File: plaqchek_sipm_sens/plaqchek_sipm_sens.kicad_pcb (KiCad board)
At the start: 2 copper layers, 90 parts, among them J2 Conn_01x04, J3 Conn_01x05, U1 TPS7A2050PDBVR, U10 AFBR-S4N44P014M, U11 LDK320AM-R, U2 OPA863A, U3 OPA863A, U4 OPA863A, U5 MCP1501T-50E, U6 MCP33131-10-E/MS, U7 MIC5504-1.8YM5, U8 RT9072BGB, U9 MC79M05_TO252

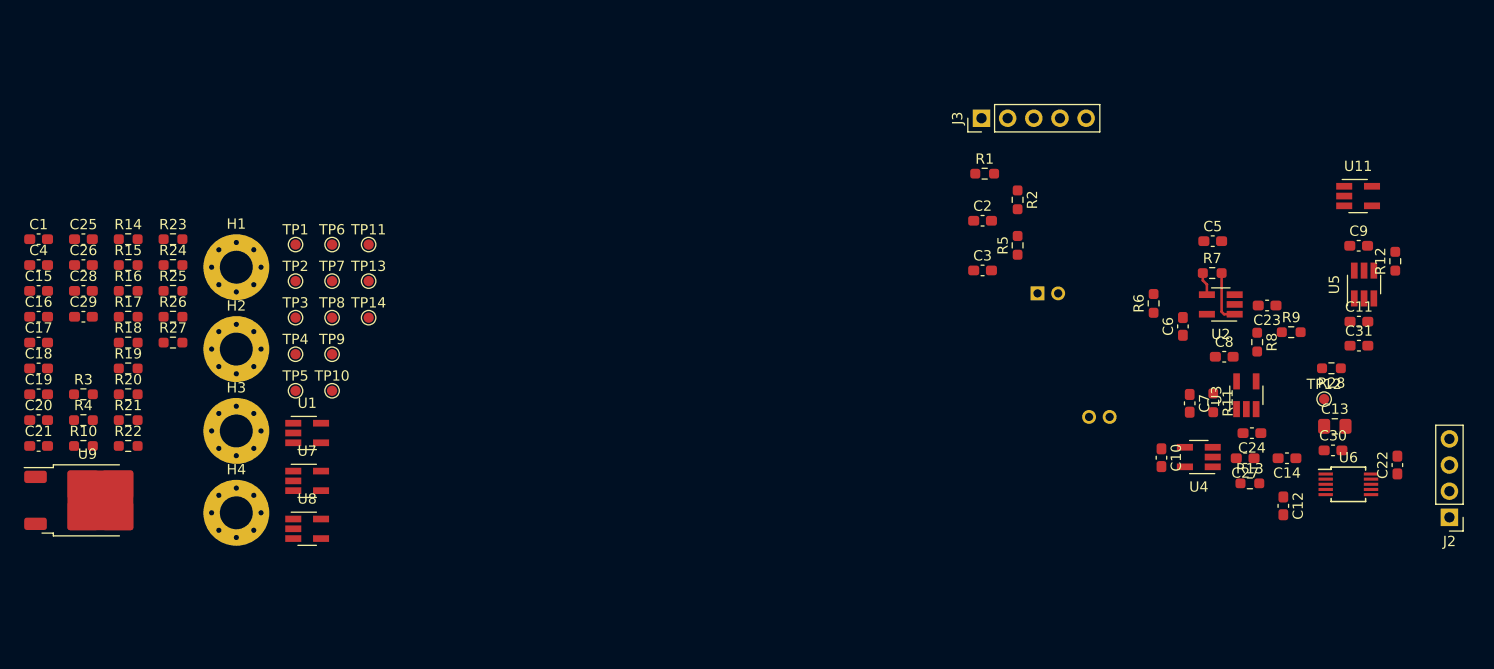
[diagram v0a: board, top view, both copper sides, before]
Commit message: start sensor board routing
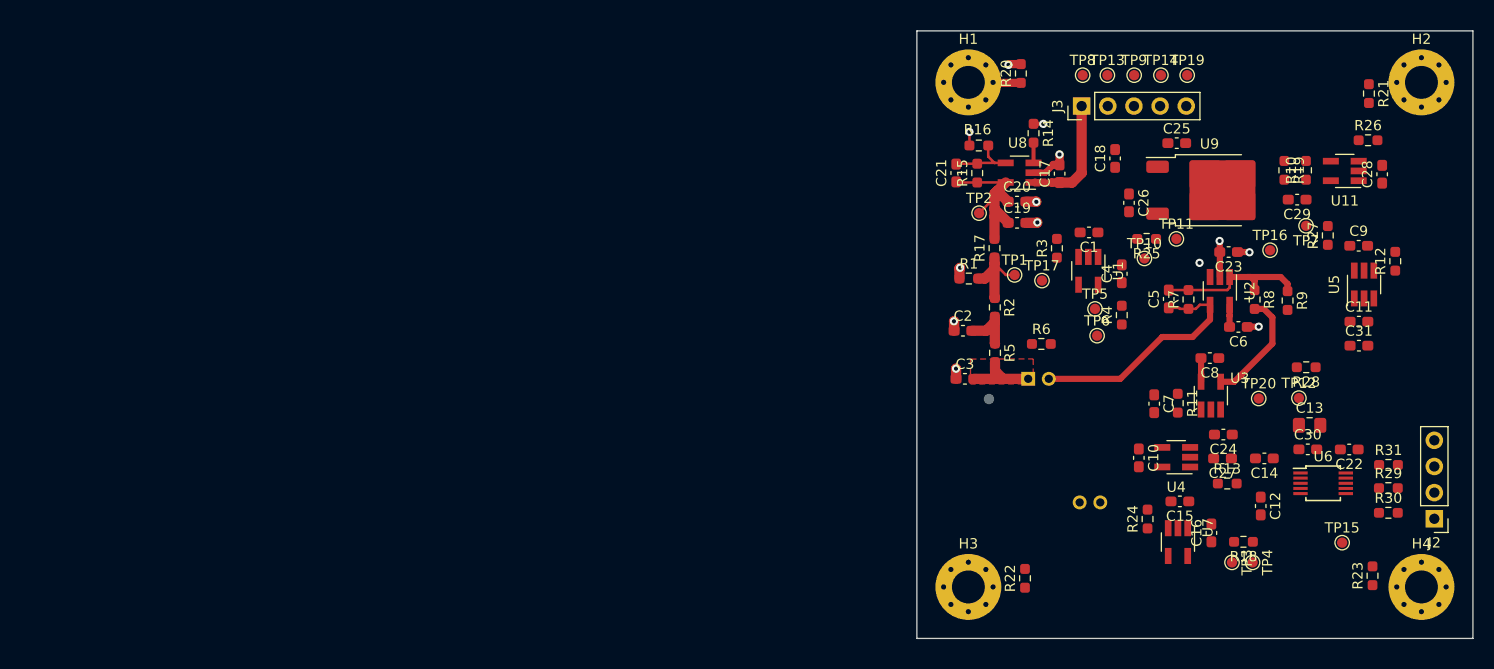
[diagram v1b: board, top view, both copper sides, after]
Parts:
- added R29: 0R, Resistor_SMD:R_0603_1608Metric_Pad0.98x0.95mm_HandSolder, F.Cu at (196.8, 101.4)
- added R30: 0R, Resistor_SMD:R_0603_1608Metric_Pad0.98x0.95mm_HandSolder, F.Cu at (196.8, 103.8)
- added R31: 0R, Resistor_SMD:R_0603_1608Metric_Pad0.98x0.95mm_HandSolder, F.Cu at (196.8, 99.2)
- added TP15: TestPoint, TestPoint:TestPoint_Pad_D1.0mm, F.Cu at (192.3, 106.7)
- added TP16: TestPoint, TestPoint:TestPoint_Pad_D1.0mm, F.Cu at (185.3, 78.3)
- added TP17: TestPoint, TestPoint:TestPoint_Pad_D1.0mm, F.Cu at (163.2, 81.2)
- added TP18: TestPoint, TestPoint:TestPoint_Pad_D1.0mm, B.Cu at (158.0, 92.8)
- added TP19: TestPoint, TestPoint:TestPoint_Pad_D1.0mm, F.Cu at (177.2, 61.3)
- added TP20: TestPoint, TestPoint:TestPoint_Pad_D1.0mm, F.Cu at (184.2, 92.7)
- moved C28 126.6 mm to (196.2, 70.9), turned to 90 degrees
- moved R21 124.6 mm to (194.9, 63.1), turned to -90 degrees
- moved R10 121.7 mm to (188.8, 70.5), turned to 90 degrees
- moved R23 121.0 mm to (195.2, 109.9), turned to 90 degrees
- moved C29 118.4 mm to (187.9, 73.4), turned to 180 degrees
- moved H2 118.0 mm to (200.0, 62.0)
- moved R26 117.3 mm to (194.8, 67.6)
- moved C16 115.8 mm to (179.6, 105.8), turned to 90 degrees
- moved H4 115.3 mm to (200.0, 111.0)
- moved R19 113.9 mm to (186.7, 70.5), turned to -90 degrees
- moved U9 113.0 mm to (179.4, 72.5)
- moved C15 112.7 mm to (176.5, 102.7), turned to 180 degrees
- moved R27 112.6 mm to (190.9, 76.9), turned to 90 degrees
- moved R18 110.0 mm to (182.7, 106.6), turned to 180 degrees
- moved C25 106.6 mm to (176.2, 67.9)
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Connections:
- net Net-(U1-OUT) renamed /5V_OUT
- net Net-(U11-OUT) renamed /5V35_OUT
- net Net-(U7-VOUT) renamed /1V8_OUT
- net Net-(U8-VOUT) renamed /PD_BIAS_OUT
- net Net-(U9-VO) renamed /-5V_OUT
- U6 pad 6: SPI_3V3_ADC_CS -> Net-(U6-CNVST)
- U6 pad 7: SPI_3V3_ADC_MISO -> Net-(U6-SDO)
- U6 pad 8: SPI_3V3_ADC_SCLK -> Net-(U6-SCLK)
- U8 pad 3: (no net) -> Net-(U8-SHDN)
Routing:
- net /SIPM Readout/SIPM_OUT: track 2.27 -> 23.7 mm
- net /PD_BIAS_OUT: track 0.00 -> 16.3 mm
- net GND: track 0.00 -> 14.8 mm, vias 0 -> 12
- net SIPM_BIAS_OUT: track 0.00 -> 11.6 mm
- net Net-(U3--): track 0.00 -> 11.2 mm
- net Net-(U2-OUT): track 5.13 -> 15.4 mm
- net PD_BIAS: track 0.00 -> 8.31 mm
- net /SIPM Readout/SIPM_BIAS: track 0.00 -> 7.21 mm
- net Net-(U8-FB): track 0.00 -> 6.82 mm
- net Net-(H1-Pad1): track 0.00 -> 5.18 mm
- net Net-(C2-Pad2): track 0.00 -> 5.17 mm
- net +5VA: track 0.00 -> 4.46 mm
- net -5VA: track 0.00 -> 3.51 mm, vias 0 -> 1
- net Net-(U8-SHDN): track 0.00 -> 1.97 mm
- added copper zone on F.Cu, net /SIPM Readout/SIPM_BIAS
- added copper zone on F.Cu, net SIPM_BIAS_OUT
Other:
- board outline added: 54 x 59 mm

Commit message: finish routing sipm board
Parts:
- H1, H2, H3, H4: footprint MountingHole:MountingHole_3.2mm_M3_Pad_Via -> MountingHole:MountingHole_3.2mm_M3_Pad
- moved TP6 16.7 mm to (182.4, 77.2)
- moved C25 13.4 mm to (188.1, 61.8)
- moved C2 13.1 mm to (164.2, 76.4), turned to -90 degrees
- moved R4 12.9 mm to (178.7, 74.4), turned to 180 degrees
- moved TP5 12.0 mm to (177.4, 76.3)
- moved R12 12.0 mm to (191.6, 89.8), turned to -90 degrees
- moved C11 12.0 mm to (188.1, 95.7)
- moved C31 12.0 mm to (188.1, 98.0)
- moved U5 12.0 mm to (188.6, 92.1)
- moved R27 11.8 mm to (185.6, 87.4)
- moved C9 11.8 mm to (188.4, 88.3)
- moved TP11 11.6 mm to (187.0, 72.9)
- moved R19 10.9 mm to (182.4, 80.5)
- moved C28 10.8 mm to (192.1, 80.9)
- moved R10 10.8 mm to (184.7, 80.6)
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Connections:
- R12 pad 1: Net-(U5-~{SHDN}) -> +5.35V
- R12 pad 2: +5.35V -> Net-(U5-~{SHDN})
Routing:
- net GND: track 14.8 -> 56.5 mm, vias 12 -> 96
- net Net-(U3-OUT): track 0.00 -> 34.7 mm, vias 0 -> 2
- net -6V5: track 0.00 -> 26.2 mm
- net +6V: track 0.00 -> 21.6 mm, vias 0 -> 4
- net /SIPM Readout/VREF_ADC: track 0.00 -> 14.5 mm
- net +3V3: track 0.00 -> 13.0 mm, vias 0 -> 4
- net +5.35V: track 0.00 -> 12.5 mm, vias 0 -> 2
- net /5V35_OUT: track 0.00 -> 11.6 mm
- net -5VA: track 3.51 -> 13.4 mm, vias 1 -> 6
- net +5VA: track 4.46 -> 14.2 mm, vias 0 -> 6
- net +1V8: track 0.00 -> 8.22 mm, vias 0 -> 4
- net /SIPM Readout/AIN: track 0.00 -> 8.10 mm
- net /1V8_OUT: track 0.00 -> 7.47 mm
- net /SIPM Readout/SIPM_BIAS: track 7.21 -> 0.00 mm
- net Net-(U5-OUT): track 0.00 -> 7.14 mm
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- added copper zone on F.Cu, net +1V8
- added copper zone on In2.Cu, net +1V8
- added copper zone on F.Cu, net +3V3
- added copper zone on In2.Cu, net +3V3
- added copper zone on F.Cu, net +5VA
- added copper zone on In2.Cu, net +5VA
- added copper zone on F.Cu, net +6V
- added copper zone on In2.Cu, net +6V
- added copper zone on F.Cu, net -5VA
- added copper zone on In2.Cu, net -5VA
- added copper zone on F.Cu, net -6V5
- added copper zone on F.Cu, net /-5V_OUT
- added copper zone on F.Cu, net /5V35_OUT
- added copper zone on F.Cu, net /SIPM Readout/VREF_ADC
- added copper zone on B.Cu, net GND
- added copper zone on F.Cu, net GND
- added copper zone on In1.Cu, net GND
- added copper zone on In2.Cu, net GND
- added copper zone on F.Cu, net PD_BIAS
- removed copper zone on F.Cu, net SIPM_BIAS_OUT
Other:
- board size 54 x 59 mm -> 51 x 59 mm
- copper layers 2 -> 4
- board text added: "+6V"
- board text added: "-6V5"
- board text added: "3V3"
- board text added: "FYDP TEAM #12 JAN 2024"
- board text added: "GND"
- board text added: "PHOTOSENSING"
- board text added: "PLAQCHEK"
- board text added: "SIPM 44V"

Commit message: finish all pcbs, generate gerber files
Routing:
- net GND: vias 96 -> 176
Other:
- board text added: "ADC OUT"
- board text added: "CLK"
- board text added: "CS"
- board text added: "FYDP TEAM #12 JAN 2025"
- board text added: "MISO"
- board text removed: "FYDP TEAM #12 JAN 2024"
